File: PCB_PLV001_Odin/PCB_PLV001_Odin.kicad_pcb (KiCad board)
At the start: 2 copper layers, 101 parts, among them J1 PWR/CAN/QB, J2 IMU, J3 INS, J4 ROT1, J5 ROT2, Q1 DMG2302UK-7, Q2 DMP2123L-7, U1 74HC21, U10 SN65HVD232, U2 74HC266, U3 74HC08, U4 74HC21, U5 74LVC1G17, U6 LTC6993xS6-1, U7 R-78B12-2.0, U8 MAX3221, U9 MAX3221

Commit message: Odin routing
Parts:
- added REF**: MountingHole_3.2mm_M3, MountingHole:MountingHole_3.2mm_M3, F.Cu at (172.0, 57.0)
- added REF**: MountingHole_3.2mm_M3, MountingHole:MountingHole_3.2mm_M3, F.Cu at (172.0, 149.0)
- added REF**: MountingHole_3.2mm_M3, MountingHole:MountingHole_3.2mm_M3, F.Cu at (105.0, 149.0)
- added REF**: MountingHole_3.2mm_M3, MountingHole:MountingHole_3.2mm_M3, F.Cu at (105.0, 57.0)
- C1, FB1: moved to F.Cu
- C13, C14, C15, C16, C17, C18, C19, C2, C20, C22, C27, C28, C5, C7, D6, D7, JP1, Q1, Q2, R1, R10, R11, R12, R14, R15, R16, R17, R18, R19, R2, R20, R21, R22, R23, R24, R25, R3, R30, R31, R32, R33, R39, R4, R5, R6, R7, R8, R9, U1, U10, U2, U3, U4, U5, U6, U8, U9: moved to B.Cu
- moved J3 104.2 mm to (154.5, 143.5), turned to 180 degrees
- moved R7 103.4 mm to (117.5, 98.0)
- moved R1 100.9 mm to (121.5, 92.0), turned to 180 degrees
- moved R21 100.1 mm to (142.2, 129.1)
- moved D7 98.2 mm to (159.2, 119.5), turned to 180 degrees
- moved R33 97.5 mm to (159.2, 122.0), turned to 180 degrees
- moved R8 97.5 mm to (117.5, 101.0)
- moved R6 95.1 mm to (117.5, 95.0)
- moved R3 94.4 mm to (121.5, 98.0), turned to 180 degrees
- moved D6 94.3 mm to (154.8, 119.5), turned to 180 degrees
- moved C23 94.2 mm to (118.2, 115.2), turned to 90 degrees
- moved R32 93.4 mm to (154.8, 122.0), turned to 180 degrees
- moved R12 92.2 mm to (143.5, 106.2), turned to 270 degrees
- moved C29 91.5 mm to (164.0, 143.5), turned to 270 degrees
- moved C7 90.8 mm to (143.5, 110.2), turned to 270 degrees
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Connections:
- C3 pad 1: +3V3 -> +5V
- C4 pad 1: +3V3 -> +5V
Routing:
- net +5V: track 0.00 -> 206.4 mm, vias 0 -> 11
- net +12V: track 0.00 -> 183.1 mm, vias 0 -> 2
- net /HEARTBEAT_BUFF: track 0.00 -> 172.5 mm, vias 0 -> 2
- net +3V3: track 0.00 -> 126.7 mm, vias 0 -> 2
- net /MCU_QB_INPUT: track 0.00 -> 121.8 mm, vias 0 -> 1
- net /ROT1_PPS2: track 0.00 -> 117.5 mm, vias 0 -> 1
- net /ROT1_PPS1: track 0.00 -> 113.9 mm, vias 0 -> 1
- net /ROT1_PPS5: track 0.00 -> 108.0 mm, vias 0 -> 3
- net /HEARTBEAT_ADDRESS_4: track 0.00 -> 106.2 mm, vias 0 -> 2
- net /ROT2_PPS3: track 0.00 -> 103.3 mm, vias 0 -> 3
- net /INS_PPS: track 0.00 -> 80.4 mm
- net /ROT1_PPS3: track 0.00 -> 77.2 mm, vias 0 -> 2
- net /HEARTBEAT_RESTART: track 0.00 -> 77.2 mm, vias 0 -> 2
- net /ROT1_PPS4: track 0.00 -> 77.0 mm, vias 0 -> 2
- net /HEARTBEAT_ADDRESS_3: track 0.00 -> 76.9 mm
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- added copper zone on F.Cu, net +12V
- added copper zone on B.Cu, net +24V
- added copper zone on F.Cu, net +24V
- added copper zone on F.Cu, net /VIN
- added copper zone on B.Cu, net GND
- added copper zone on F.Cu, net GND
- added copper zone on B.Cu, net Net-(C30-Pad1)
- added copper zone on F.Cu, net Net-(C30-Pad1)
- added copper zone on F.Cu, net Net-(D1-Pad2)
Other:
- board outline added: 75 x 100 mm

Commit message: Fix transistors in heartbeat circuits
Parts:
- D2: value GREEN -> QB_IN
- D3: value BLUE -> QB_OUT
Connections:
- Q1 pad 2: Net-(Q1-Pad2) -> GND
- Q1 pad 3: GND -> Net-(Q1-Pad3)
- Q2 pad 1: Net-(Q1-Pad2) -> Net-(Q1-Pad3)
- R12 pad 2: Net-(Q1-Pad2) -> Net-(Q1-Pad3)
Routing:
- net Net-(Q1-Pad3): track 0.00 -> 8.25 mm
- net Net-(Q1-Pad2): track 4.38 -> 0.00 mm
- net GND: track 18.4 -> 20.2 mm, vias 39 -> 52
- net +12V: track 183.1 -> 184.3 mm

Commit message: Odin Silk, finish Yggdrasil component selection
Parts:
- added G***: LOGO, BoringFootprints:Paradigm_NameBelow_12.7mm, B.Cu at (131.2, 82.5)
- added G***: LOGO, BoringFootprints:Paradigm_NameBelow_25.4mm, F.Cu at (154.8, 122.5)
- added REF**: Paradigm_Title_Block, BoringFootprints:Paradigm_Title_Block, B.Cu at (173.2, 79.2)
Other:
- board text added: "Odin Navigation Board"
- board text added: "PLV001_Odin"
- board text added: "Paradigm Boring"

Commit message: Add 3D models for connectors to Odin
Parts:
- moved REF** 0.75 mm to (172.5, 79.2)
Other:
- board text added: "A"
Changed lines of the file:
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@@
   (general
     (thickness 1.6)
-    (drawings 7)
+    (drawings 8)
     (tracks 974)
     (zones 0)
@@
   )
   (module BoringFootprints:Paradigm_Title_Block (layer B.Cu)
-    (at 173.25 79.25 270)
+    (at 172.5 79.25 270)
     (fp_text reference REF** (at 0 -4.5 270) (layer B.Fab)
       (effects (font (size 1 1) (thickness 0.15)) (justify mirror))
@@
       (rotate (xyz 0 0 0))
     )
+    (model ${KIPARDIGMMOD}/boringlib/3dModels/MOLEX_430451200/430451200.stp
+      (offset (xyz 7.5 4 4))
+      (scale (xyz 1 1 1))
+      (rotate (xyz -90 0 180))
+    )
   )
   (module Connector_Molex:Molex_Micro-Fit_3.0_43650-0500_1x05_P3.00mm_Horizontal (layer F.Cu)
@@
       (rotate (xyz 0 0 0))
     )
+    (model ${KIPARDIGMMOD}/boringlib/3dModels/436500500.stp
+      (offset (xyz 6 4 2.5))
+      (scale (xyz 1 1 1))
+      (rotate (xyz -90 0 180))
+    )
   )
   (module Connector_Molex:Molex_Micro-Fit_3.0_43650-0500_1x05_P3.00mm_Horizontal (layer F.Cu)
@@
       (rotate (xyz 0 0 0))
     )
+    (model ${KIPARDIGMMOD}/boringlib/3dModels/436500500.stp
+      (offset (xyz 6 4 2.5))
+      (scale (xyz 1 1 1))
+      (rotate (xyz -90 0 180))
+    )
   )
   (module Connector_Molex:Molex_Micro-Fit_3.0_43045-0600_2x03_P3.00mm_Horizontal (layer F.Cu)
@@
       (rotate (xyz 0 0 0))
     )
+    (model ${KIPARDIGMMOD}/boringlib/3dModels/MOLEX_430450600/430450600.stp
+      (offset (xyz 3 4 4))
+      (scale (xyz 1 1 1))
+      (rotate (xyz -90 0 180))
+    )
   )
   (module Connector_Molex:Molex_Micro-Fit_3.0_43045-0600_2x03_P3.00mm_Horizontal (layer F.Cu)
@@
       (rotate (xyz 0 0 0))
     )
+    (model ${KIPARDIGMMOD}/boringlib/3dModels/MOLEX_430450600/430450600.stp
+      (offset (xyz 3 4 4))
+      (scale (xyz 1 1 1))
+      (rotate (xyz -90 0 180))
+    )
   )
   (module Jumper:SolderJumper-2_P1.3mm_Open_RoundedPad1.0x1.5mm (layer B.Cu)
@@
     )
   )
+  (gr_text A (at 172.25 87.25 90) (layer B.SilkS)
+    (effects (font (size 0.9 0.9) (thickness 0.1)) (justify mirror))
+  )
   (gr_text "Paradigm Boring" (at 128.5 126.25) (layer F.SilkS)
     (effects (font (size 2.75 2.75) (thickness 0.3)))
@@
     (effects (font (size 2 2) (thickness 0.3)) (justify left))
   )
-  (gr_text PLV001_Odin (at 173 78.25 90) (layer B.SilkS)
-    (effects (font (size 0.75 0.75) (thickness 0.1)) (justify mirror))
+  (gr_text PLV001_Odin (at 172.25 78.75 90) (layer B.SilkS)
+    (effects (font (size 0.9 0.9) (thickness 0.1)) (justify mirror))
   )
   (gr_line (start 101 153) (end 101 53) (layer Edge.Cuts) (width 0.05))

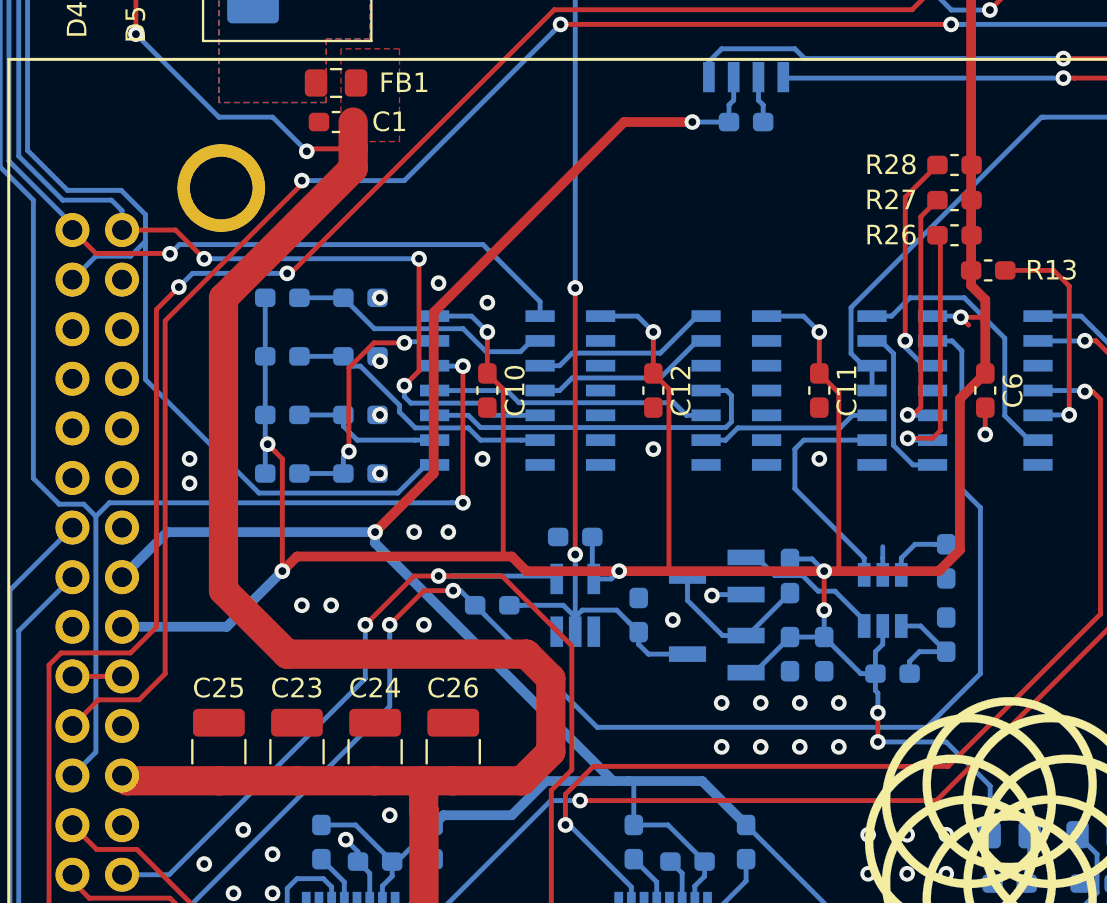
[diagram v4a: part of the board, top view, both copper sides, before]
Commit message: Make Odin pass DRC, finish Yggdrasil
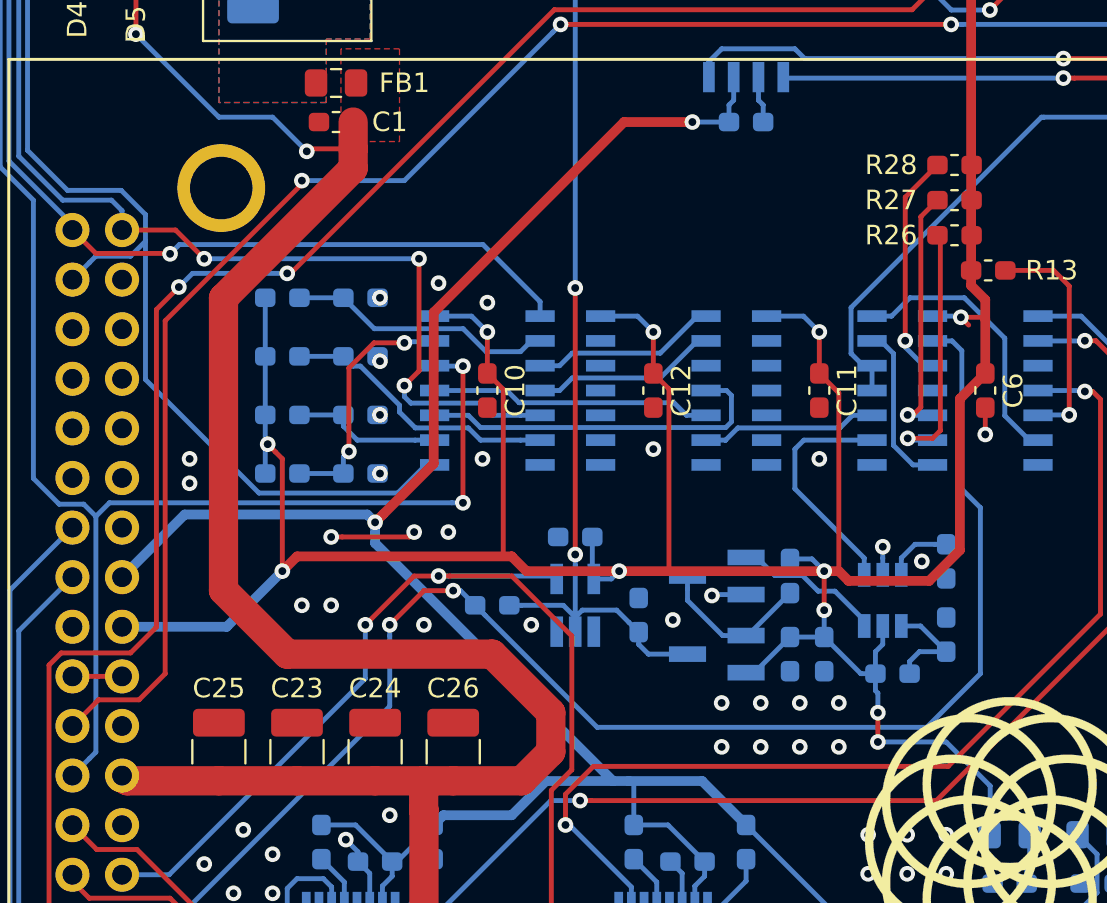
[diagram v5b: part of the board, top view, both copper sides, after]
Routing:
- net GND: track 20.2 -> 24.5 mm, vias 52 -> 56
- net +12V: track 184.3 -> 183.3 mm
- net +3V3: track 126.7 -> 127.2 mm
